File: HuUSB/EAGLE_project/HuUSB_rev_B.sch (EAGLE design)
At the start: 21 parts, among them IC1 FT245RL-REEL, IC5 74HC245D,653, IC6 74HC245D,653, IC7 ATF22V10CQZ-20PU, J1 U-M-M5SS-W-2, J2 CONN_20X2NOSILK

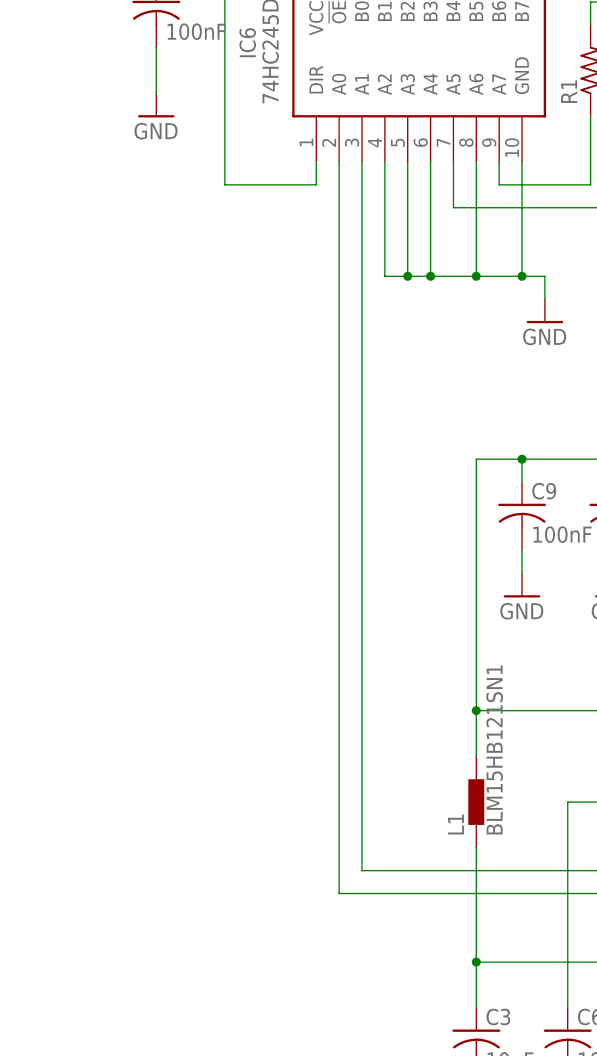
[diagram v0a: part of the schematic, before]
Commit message: Add pull-up resistors to status bits coming from FT245RL
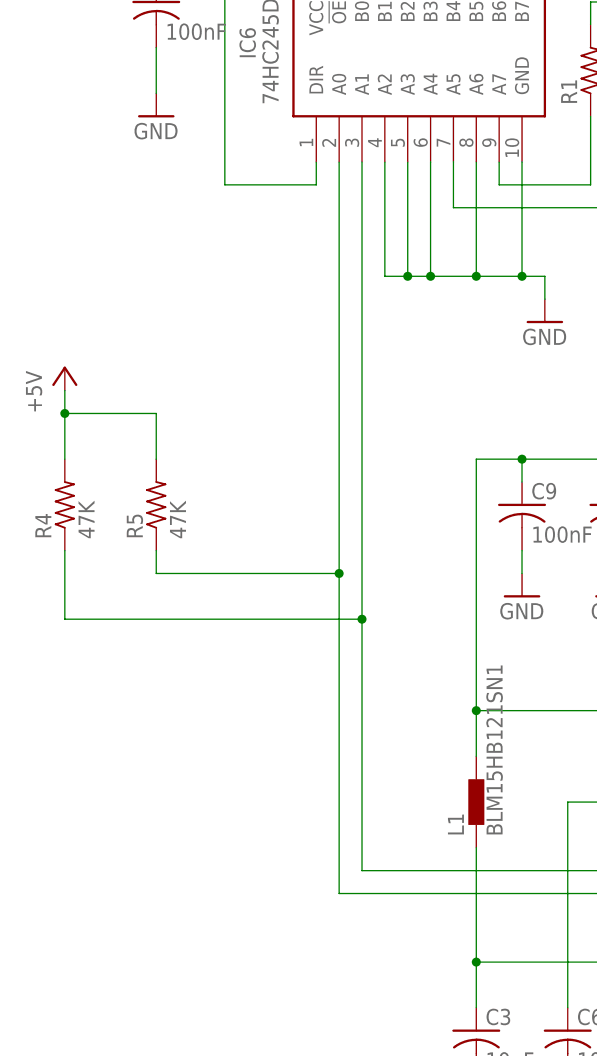
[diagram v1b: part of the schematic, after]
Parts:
- added R4, R5: 47K, resistor:R-US_R0603
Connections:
- net +5V: now also R4.2, R5.2
- net N$45: now also R4.1
- net N$46: now also R5.1
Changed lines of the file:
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@@
 <part name="C11" library="resistor" library_urn="urn:adsk.eagle:library:348" deviceset="C-US" device="C0603" package3d_urn="urn:adsk.eagle:package:23616/2" value="1uF"/>
 <part name="GND15" library="supply1" library_urn="urn:adsk.eagle:library:371" deviceset="GND" device=""/>
+<part name="R4" library="resistor" library_urn="urn:adsk.eagle:library:348" deviceset="R-US_" device="R0603" package3d_urn="urn:adsk.eagle:package:23555/3" value="47K"/>
+<part name="R5" library="resistor" library_urn="urn:adsk.eagle:library:348" deviceset="R-US_" device="R0603" package3d_urn="urn:adsk.eagle:package:23555/3" value="47K"/>
+<part name="P+3" library="supply1" library_urn="urn:adsk.eagle:library:371" deviceset="+5V" device=""/>
 </parts>
 <sheets>
@@
 <instance part="GND15" gate="1" x="279.4" y="129.54" smashed="yes">
 <attribute name="VALUE" x="276.86" y="127" size="1.778" layer="96"/>
+</instance>
+<instance part="R4" gate="G$1" x="50.8" y="76.2" smashed="yes" rot="R90">
+<attribute name="NAME" x="49.3014" y="72.39" size="1.778" layer="95" rot="R90"/>
+<attribute name="VALUE" x="54.102" y="72.39" size="1.778" layer="96" rot="R90"/>
+</instance>
+<instance part="R5" gate="G$1" x="60.96" y="76.2" smashed="yes" rot="R90">
+<attribute name="NAME" x="59.4614" y="72.39" size="1.778" layer="95" rot="R90"/>
+<attribute name="VALUE" x="64.262" y="72.39" size="1.778" layer="96" rot="R90"/>
+</instance>
+<instance part="P+3" gate="1" x="50.8" y="91.44" smashed="yes">
+<attribute name="VALUE" x="48.26" y="86.36" size="1.778" layer="96" rot="R90"/>
 </instance>
 </instances>
@@
 <wire x1="195.58" y1="269.24" x2="187.96" y2="269.24" width="0.1524" layer="91"/>
 <junction x="187.96" y="269.24"/>
+</segment>
+<segment>
+<pinref part="P+3" gate="1" pin="+5V"/>
+<pinref part="R4" gate="G$1" pin="2"/>
+<wire x1="50.8" y1="88.9" x2="50.8" y2="86.36" width="0.1524" layer="91"/>
+<wire x1="50.8" y1="86.36" x2="50.8" y2="81.28" width="0.1524" layer="91"/>
+<wire x1="50.8" y1="86.36" x2="60.96" y2="86.36" width="0.1524" layer="91"/>
+<junction x="50.8" y="86.36"/>
+<pinref part="R5" gate="G$1" pin="2"/>
+<wire x1="60.96" y1="86.36" x2="60.96" y2="81.28" width="0.1524" layer="91"/>
 </segment>
 </net>
@@
 <wire x1="142.24" y1="35.56" x2="83.82" y2="35.56" width="0.1524" layer="91"/>
 <pinref part="IC6" gate="G$1" pin="A1"/>
-<wire x1="83.82" y1="35.56" x2="83.82" y2="114.3" width="0.1524" layer="91"/>
+<wire x1="83.82" y1="35.56" x2="83.82" y2="63.5" width="0.1524" layer="91"/>
+<pinref part="R4" gate="G$1" pin="1"/>
+<wire x1="83.82" y1="63.5" x2="83.82" y2="114.3" width="0.1524" layer="91"/>
+<wire x1="50.8" y1="71.12" x2="50.8" y2="63.5" width="0.1524" layer="91"/>
+<wire x1="50.8" y1="63.5" x2="83.82" y2="63.5" width="0.1524" layer="91"/>
+<junction x="83.82" y="63.5"/>
 </segment>
 </net>
@@
 <wire x1="144.78" y1="33.02" x2="81.28" y2="33.02" width="0.1524" layer="91"/>
 <pinref part="IC6" gate="G$1" pin="A0"/>
-<wire x1="81.28" y1="33.02" x2="81.28" y2="114.3" width="0.1524" layer="91"/>
-</segment>
-</net>
+<wire x1="81.28" y1="33.02" x2="81.28" y2="68.58" width="0.1524" layer="91"/>
+<pinref part="R5" gate="G$1" pin="1"/>
+<wire x1="81.28" y1="68.58" x2="81.28" y2="114.3" width="0.1524" layer="91"/>
+<wire x1="60.96" y1="71.12" x2="60.96" y2="68.58" width="0.1524" layer="91"/>
+<wire x1="60.96" y1="68.58" x2="81.28" y2="68.58" width="0.1524" layer="91"/>
+<junction x="81.28" y="68.58"/>
+</segment>
+</net>
